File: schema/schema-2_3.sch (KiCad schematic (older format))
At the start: 10 parts, among them J1 Conn_01x04_Male, J2 Conn_01x04_Male, J3 Conn_01x05_Male

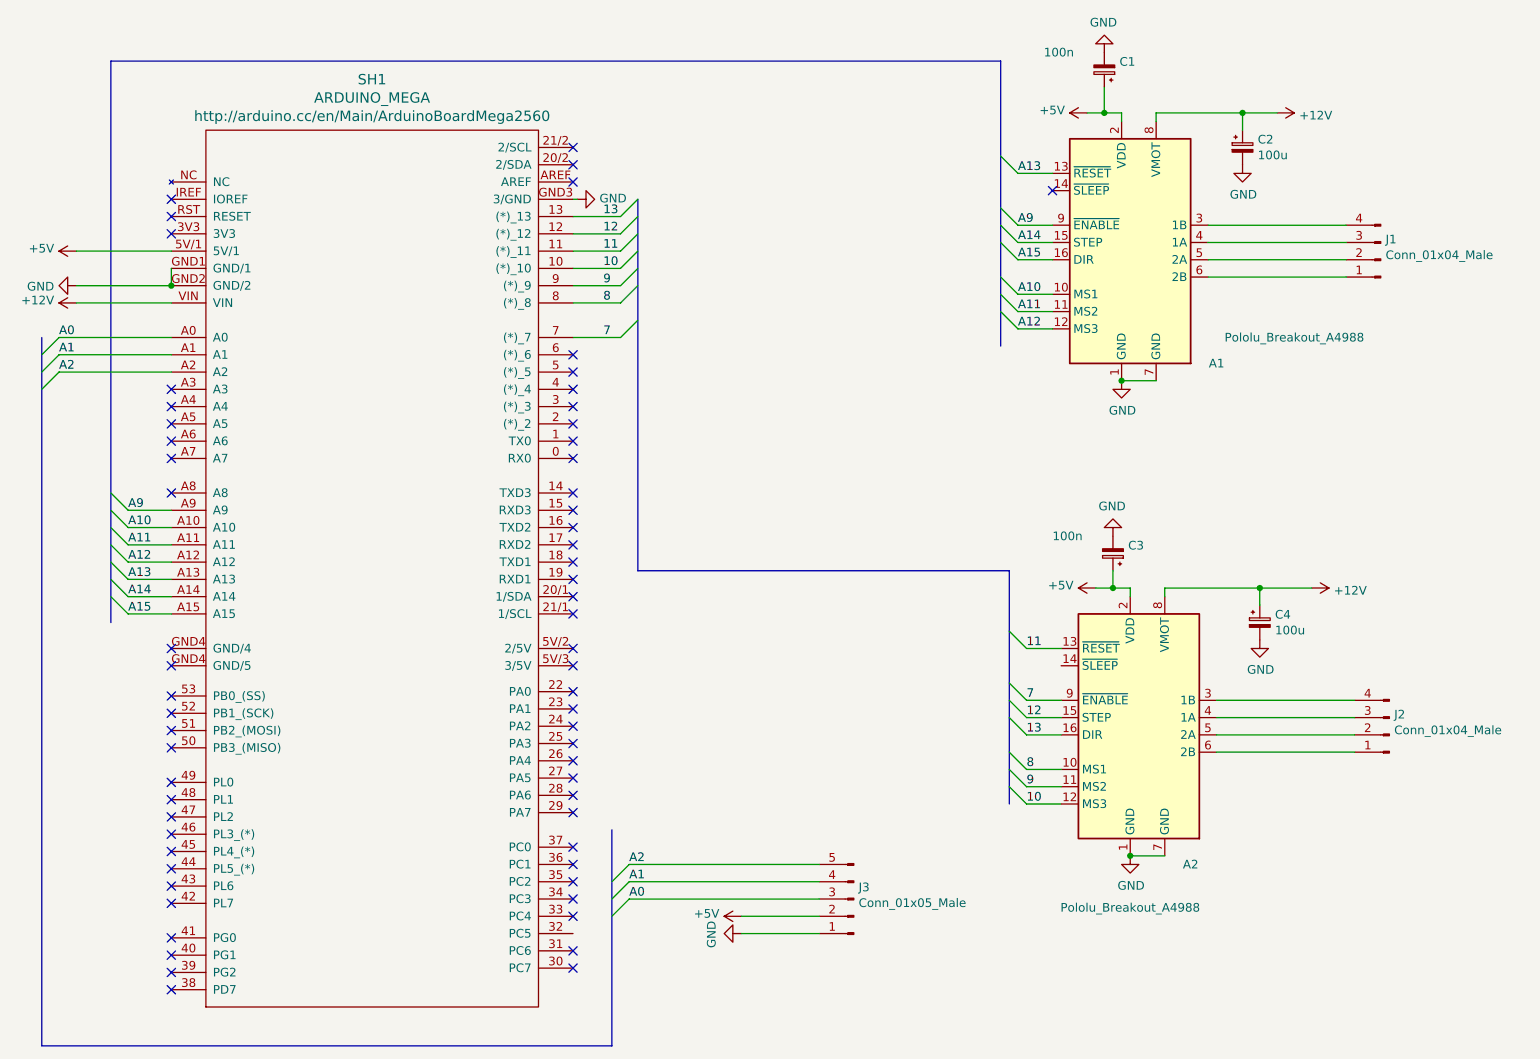
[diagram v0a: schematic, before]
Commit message: Changement des noms de version Ajout de la macro python freeroute.py
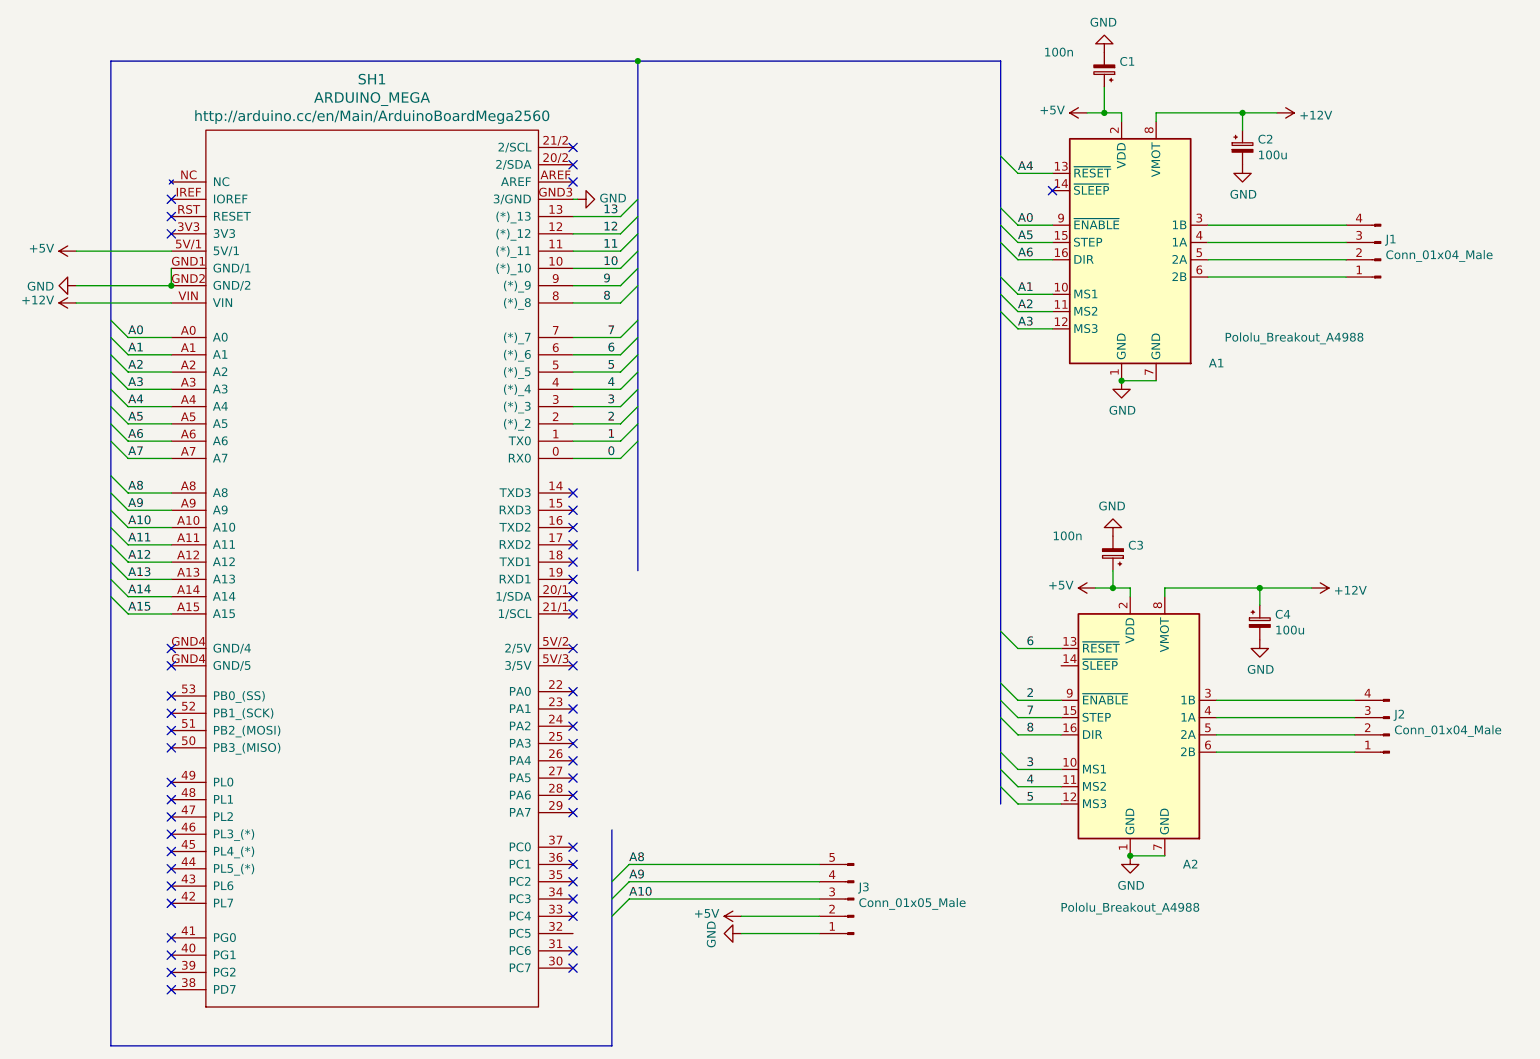
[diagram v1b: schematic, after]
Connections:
- net 10: no longer A2.12 (MS3)
- net 11: no longer A2.13 (~RESET)
- net 12: no longer A2.15 (STEP)
- net 13: no longer A2.16 (DIR)
- net 7: now also A2.15 (STEP); no longer A2.9 (~ENABLE)
- net 8: now also A2.16 (DIR); no longer A2.10 (MS1)
- net 9: no longer A2.11 (MS2)
- net A0: now also A1.9 (~ENABLE); no longer J3.3 (Pin_3)
- net A1: now also A1.10 (MS1); no longer J3.4 (Pin_4)
- net A10: now also J3.3 (Pin_3); no longer A1.10 (MS1)
- net A11: no longer A1.11 (MS2)
- net A12: no longer A1.12 (MS3)
- net A13: no longer A1.13 (~RESET)
- net A14: no longer A1.15 (STEP)
- net A15: no longer A1.16 (DIR)
- net A2: now also A1.11 (MS2); no longer J3.5 (Pin_5)
- net A9: now also J3.4 (Pin_4); no longer A1.9 (~ENABLE)
- net 0: now reaches SH1.0 (RX0)
- net 1: now reaches SH1.1 (TX0)
- net 2: now reaches SH1.2 ((*)_2)
- net 2: now also A2.9 (~ENABLE)
- net 3: now reaches SH1.3 ((*)_3)
- net 3: now also A2.10 (MS1)
- net 4: now reaches SH1.4 ((*)_4)
- net 4: now also A2.11 (MS2)
- net 5: now reaches SH1.5 ((*)_5)
- net 5: now also A2.12 (MS3)
- net 6: now reaches SH1.6 ((*)_6)
- net 6: now also A2.13 (~RESET)
- net A3: now reaches SH1.A3
- net A3: now also A1.12 (MS3)
- net A4: now reaches SH1.A4
- net A4: now also A1.13 (~RESET)
- net A5: now reaches SH1.A5
- net A5: now also A1.15 (STEP)
- net A6: now reaches SH1.A6
- net A6: now also A1.16 (DIR)
- net A7: now reaches SH1.A7
- net A8: now reaches SH1.A8
- net A8: now also J3.5 (Pin_5)
- no-connect marks 63 -> 50
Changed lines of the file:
@@
 A15
 Wire Bus Line
-	1750 900  6900 900
+	1750 900  4800 900
 Entry Wire Line
 	6900 1750 7000 1850
@@
 	7000 2450 7200 2450
 Text Label 7000 1850 0    50   ~ 0
-A9
+A0
 Text Label 7000 2250 0    50   ~ 0
-A10
+A1
 Text Label 7000 2350 0    50   ~ 0
-A11
+A2
 Text Label 7000 2450 0    50   ~ 0
-A12
+A3
 Text Label 7000 1950 0    50   ~ 0
-A14
+A5
 Text Label 7000 2050 0    50   ~ 0
-A15
+A6
 Text Label 7000 1550 0    50   ~ 0
-A13
+A4
 Entry Wire Line
 	4700 1800 4800 1700
@@
 	4425 1900 4700 1900
 Entry Wire Line
-	7050 4300 6950 4200
-Entry Wire Line
-	7050 4600 6950 4500
-Entry Wire Line
-	7050 4700 6950 4600
-Entry Wire Line
-	7050 4800 6950 4700
-Entry Wire Line
-	7050 5000 6950 4900
-Entry Wire Line
-	7050 5100 6950 5000
-Entry Wire Line
-	7050 5200 6950 5100
-Wire Wire Line
-	7050 5200 7250 5200
-Wire Wire Line
-	7250 5100 7050 5100
-Wire Wire Line
-	7050 5000 7250 5000
-Wire Wire Line
-	7250 4800 7050 4800
-Wire Wire Line
-	7050 4700 7250 4700
-Wire Wire Line
-	7250 4600 7050 4600
-Wire Wire Line
-	7050 4300 7250 4300
+	7000 4300 6900 4200
+Entry Wire Line
+	7000 4600 6900 4500
+Entry Wire Line
+	7000 4700 6900 4600
+Entry Wire Line
+	7000 4800 6900 4700
+Entry Wire Line
+	7000 5000 6900 4900
+Entry Wire Line
+	7000 5100 6900 5000
+Entry Wire Line
+	7000 5200 6900 5100
 Text Label 4600 1800 0    50   ~ 0
 13
@@
 Text Label 4600 2300 0    50   ~ 0
 8
-Text Label 4600 2500 0    50   ~ 0
+Text Label 4625 2500 0    50   ~ 0
 7
 Text Label 7050 4300 0    50   ~ 0
-11
+6
 Text Label 7050 4600 0    50   ~ 0
+2
+Text Label 7050 5000 0    50   ~ 0
+3
+Text Label 7050 5100 0    50   ~ 0
+4
+Text Label 7050 5200 0    50   ~ 0
+5
+Text Label 7050 4700 0    50   ~ 0
 7
-Text Label 7050 5000 0    50   ~ 0
+Text Label 7050 4800 0    50   ~ 0
 8
-Text Label 7050 5100 0    50   ~ 0
-9
-Text Label 7050 5200 0    50   ~ 0
-10
-Text Label 7050 4700 0    50   ~ 0
-12
-Text Label 7050 4800 0    50   ~ 0
-13
 $Comp
 L power:GND #PWR02
@@
 	-1   0    0    1
 $EndComp
-Wire Bus Line
-	4800 3850 6950 3850
 $Comp
 L Device:CP_Small C3
@@
 NoConn ~ 4425 3500
 NoConn ~ 4425 3400
-NoConn ~ 4425 3200
-NoConn ~ 4425 3100
-NoConn ~ 4425 2900
-NoConn ~ 4425 2800
-NoConn ~ 4425 2700
-NoConn ~ 4425 2600
 Wire Wire Line
 	4425 1700 4450 1700
@@
 NoConn ~ 2100 1800
 NoConn ~ 2100 1900
-NoConn ~ 2100 2800
-NoConn ~ 2100 2900
-NoConn ~ 2100 3000
-NoConn ~ 2100 3100
-NoConn ~ 2100 3200
 NoConn ~ 7200 1650
 Wire Wire Line
@@
 Wire Wire Line
 	7200 1950 7000 1950
-NoConn ~ 2100 3400
-Wire Bus Line
-	1350 6600 4650 6600
 Entry Wire Line
 	4750 5750 4650 5850
@@
 	4750 5750 5850 5750
 Entry Wire Line
-	1450 2500 1350 2600
-Entry Wire Line
-	1450 2600 1350 2700
-Wire Wire Line
-	1450 2500 2100 2500
-Wire Wire Line
-	2100 2600 1450 2600
-Text Label 1450 2500 0    50   ~ 0
+	1750 2400 1850 2500
+Entry Wire Line
+	1750 2500 1850 2600
+Text Label 1850 2500 0    50   ~ 0
 A0
-Text Label 1450 2600 0    50   ~ 0
+Text Label 1850 2600 0    50   ~ 0
 A1
 Text Label 4750 5650 0    50   ~ 0
-A1
+A9
 Text Label 4750 5750 0    50   ~ 0
-A0
-Entry Wire Line
-	1350 2800 1450 2700
-Wire Wire Line
-	2100 2700 1450 2700
-Text Label 1450 2700 0    50   ~ 0
+A10
+Entry Wire Line
+	1850 2700 1750 2600
+Text Label 1850 2700 0    50   ~ 0
 A2
-NoConn ~ 4425 3000
 Text Label 4750 5550 0    50   ~ 0
-A2
+A8
+Wire Wire Line
+	2100 2500 1850 2500
+Wire Wire Line
+	2100 2600 1850 2600
+Wire Wire Line
+	2100 2700 1850 2700
 Wire Bus Line
-	1350 2500 1350 6600
+	1750 6600 4650 6600
+Entry Wire Line
+	1750 3300 1850 3400
+Wire Wire Line
+	2100 3400 1850 3400
+Text Label 1850 3400 0    50   ~ 0
+A8
+Entry Wire Line
+	1750 2700 1850 2800
+Entry Wire Line
+	1750 2800 1850 2900
+Entry Wire Line
+	1750 2900 1850 3000
+Entry Wire Line
+	1750 3000 1850 3100
+Entry Wire Line
+	1750 3100 1850 3200
+Wire Wire Line
+	2100 2800 1850 2800
+Wire Wire Line
+	1850 2900 2100 2900
+Wire Wire Line
+	2100 3000 1850 3000
+Wire Wire Line
+	1850 3100 2100 3100
+Wire Wire Line
+	2100 3200 1850 3200
+Text Label 1850 2800 0    50   ~ 0
+A3
+Text Label 1850 2900 0    50   ~ 0
+A4
+Text Label 1850 3000 0    50   ~ 0
+A5
+Text Label 1850 3100 0    50   ~ 0
+A6
+Text Label 1850 3200 0    50   ~ 0
+A7
+Entry Wire Line
+	4700 2600 4800 2500
+Entry Wire Line
+	4700 2700 4800 2600
+Entry Wire Line
+	4700 2800 4800 2700
+Entry Wire Line
+	4700 2900 4800 2800
+Entry Wire Line
+	4700 3000 4800 2900
+Entry Wire Line
+	4700 3100 4800 3000
+Entry Wire Line
+	4700 3200 4800 3100
+Wire Wire Line
+	4700 3200 4425 3200
+Wire Wire Line
+	4425 3100 4700 3100
+Wire Wire Line
+	4425 2900 4700 2900
+Wire Wire Line
+	4425 3000 4700 3000
+Wire Wire Line
+	4700 2800 4425 2800
+Wire Wire Line
+	4425 2700 4700 2700
+Wire Wire Line
+	4425 2600 4700 2600
+Text Label 4625 2600 0    50   ~ 0
+6
+Text Label 4625 2700 0    50   ~ 0
+5
+Text Label 4625 2800 0    50   ~ 0
+4
+Text Label 4625 2900 0    50   ~ 0
+3
+Text Label 4625 3000 0    50   ~ 0
+2
+Text Label 4625 3100 0    50   ~ 0
+1
+Text Label 4625 3200 0    50   ~ 0
+0
+Wire Wire Line
+	7000 4300 7250 4300
+Wire Wire Line
+	7000 4600 7250 4600
+Wire Wire Line
+	7000 4700 7250 4700
+Wire Wire Line
+	7000 4800 7250 4800
+Wire Wire Line
+	7000 5000 7250 5000
+Wire Wire Line
+	7000 5100 7250 5100
+Wire Wire Line
+	7000 5200 7250 5200
 Wire Bus Line
 	4650 5350 4650 6600
 Wire Bus Line
-	4800 1700 4800 3850
+	6900 900  6900 5200
 Wire Bus Line
-	6950 3850 6950 5200
+	4800 900  4800 3850
 Wire Bus Line
-	6900 900  6900 2550
+	1750 900  1750 6600
+Connection ~ 4800 900
 Wire Bus Line
-	1750 900  1750 4150
+	4800 900  6900 900
 $EndSCHEMATC
